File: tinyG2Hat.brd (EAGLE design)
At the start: 102.6 x 69.1 mm, 31 parts

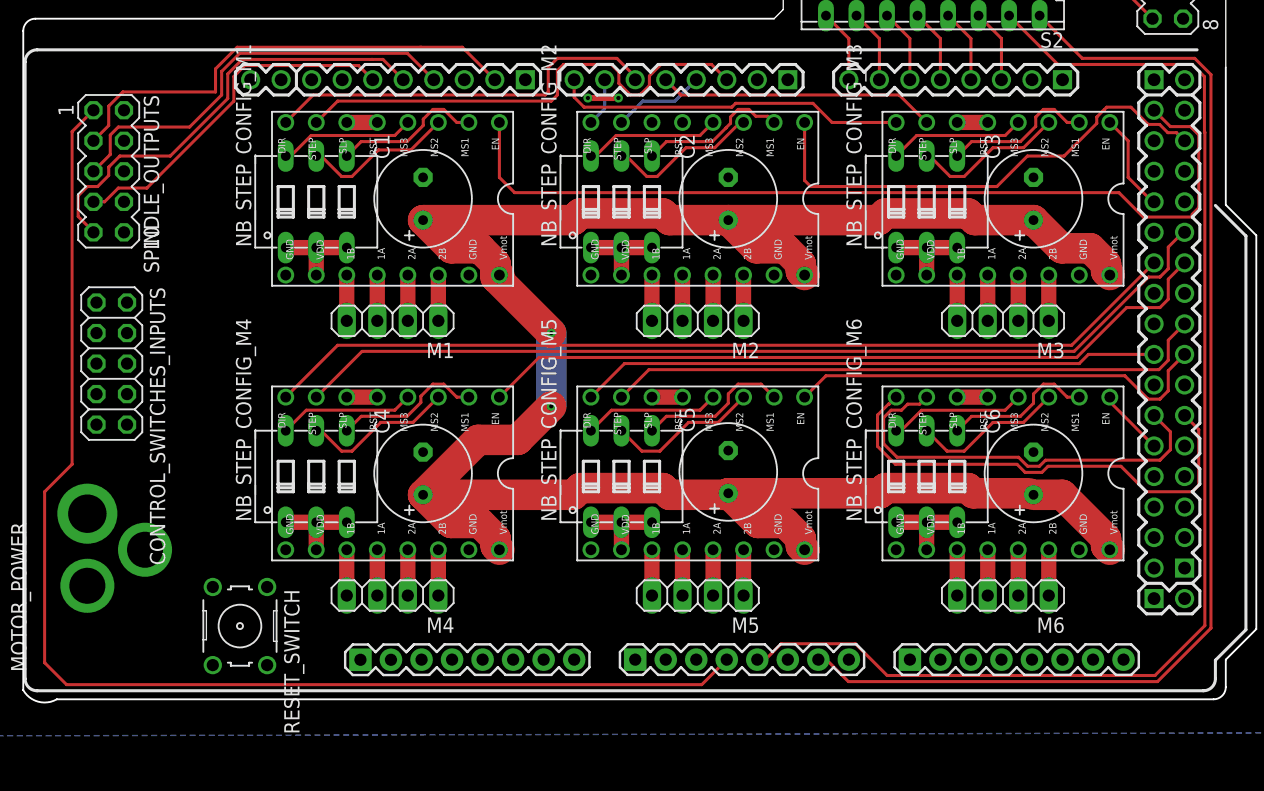
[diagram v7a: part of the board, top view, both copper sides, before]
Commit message: Routage de base terminé
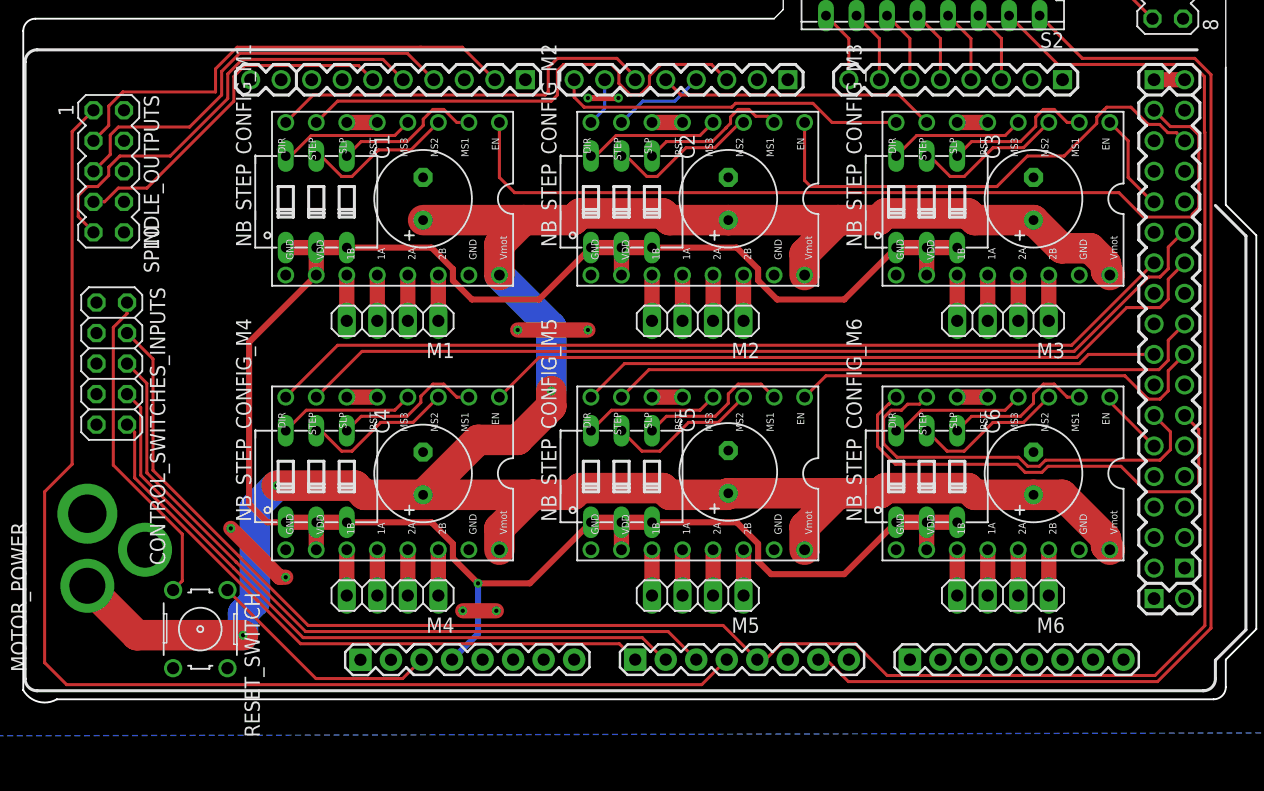
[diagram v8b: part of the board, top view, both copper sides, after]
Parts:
- moved RESET_SWITCH 3.31 mm to (14.5, 6.10)
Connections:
- net +5V: no longer ARDUINO_DUE1.5V0
- net E_STOP: now also CONTROL_SWITCHES_INPUTS.4; no longer CONTROL_SWITCHES_INPUTS.8
- net FEED_HOLD: now also CONTROL_SWITCHES_INPUTS.8; no longer CONTROL_SWITCHES_INPUTS.4
- net N$50: now also CONTROL_SWITCHES_INPUTS.2; no longer CONTROL_SWITCHES_INPUTS.10
- net SOFT_RESET: now also CONTROL_SWITCHES_INPUTS.10; no longer CONTROL_SWITCHES_INPUTS.2
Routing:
- net +3V3: track 44.2 -> 175.4 mm, vias 0 -> 1
- net E_STOP: track 104.7 -> 173.8 mm
- net CY_START: track 0.00 -> 61.9 mm
- net FEED_HOLD: track 0.00 -> 57.3 mm
- net SOFT_RESET: track 0.00 -> 52.6 mm
- net +24V: track 181.6 -> 210.6 mm, vias 2 -> 3
- net N$50: track 0.00 -> 27.1 mm
- net RESET: track 0.00 -> 19.9 mm
- net GND: track 2.54 -> 17.4 mm, vias 2 -> 8
- net +5V: track 0.00 -> 2.54 mm
- net N$10: track 0.00 -> 2.54 mm
